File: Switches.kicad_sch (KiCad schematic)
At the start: 26 parts, among them J3 INDICATOR_SWITCH_OUT

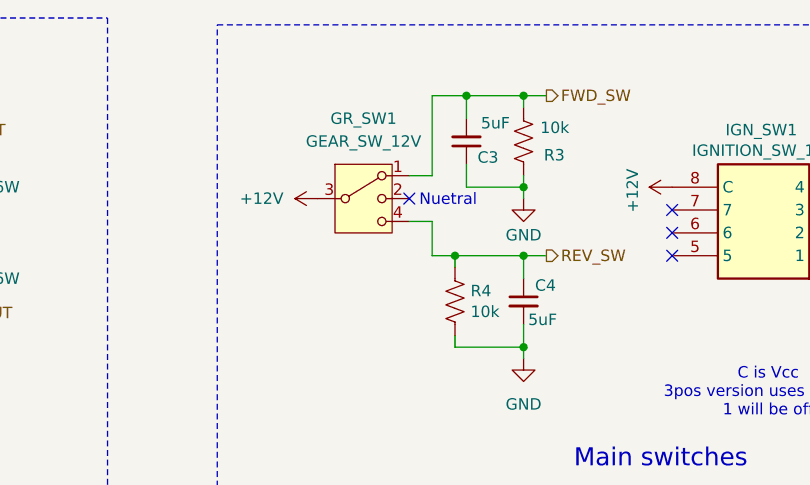
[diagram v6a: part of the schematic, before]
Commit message: Footprint all assigned, and updated to PCB
Ready for a check in to make sure everything is looking alright
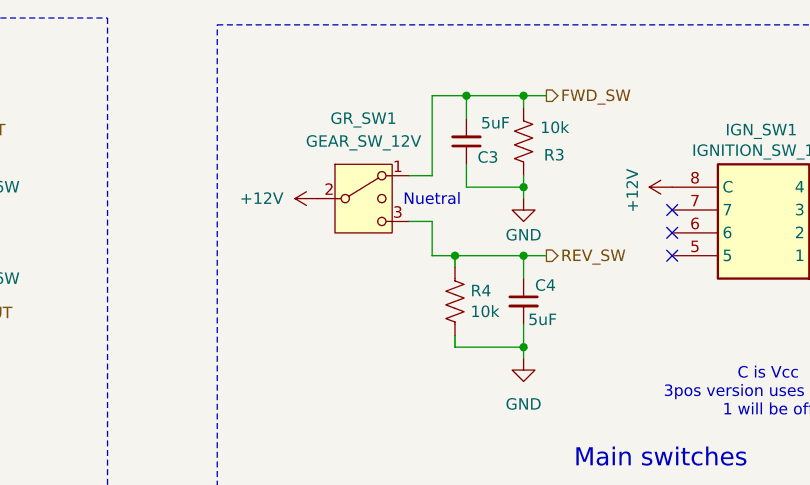
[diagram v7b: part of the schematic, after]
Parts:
- GR_SW1: symbol Switch:SW_SP3T -> Switch:SW_SPDT_MSM
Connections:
- net +12V: now also GR_SW1.2 (3); no longer GR_SW1.3
- net REV_SW: now also GR_SW1.3 (4); no longer GR_SW1.4
- no-connect marks 6 -> 5
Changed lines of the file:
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@@
 		(at 203.2 55.88)
-	)
-	(no_connect
-		(at 173.99 49.53)
 	)
 	(wire
@@
 	(text "Nuetral"
 		(exclude_from_sim no)
-		(at 178.308 49.784 0)
+		(at 176.53 49.784 0)
 		(effects
 			(font
@@
 	)
 	(symbol
-		(lib_id "Switch:SW_SP3T")
+		(lib_id "Switch:SW_SPDT_MSM")
 		(at 168.91 49.53 0)
 		(unit 1)
@@
 		)
 		(property "Footprint" "switched:SW_100_SP3T-Vertical"
-			(at 153.035 45.085 0)
+			(at 154.94 38.1 0)
 			(effects
 				(font
@@
 			)
 		)
-		(property "Description" "Switch, three position, single pole triple throw, 3 position switch, SP3T"
+		(property "Description" "Switch, single pole double throw, center OFF position"
 			(at 168.91 49.53 0)
 			(effects
@@
 		(pin "1"
 		)
-		(pin "4"
-		)
 		(instances

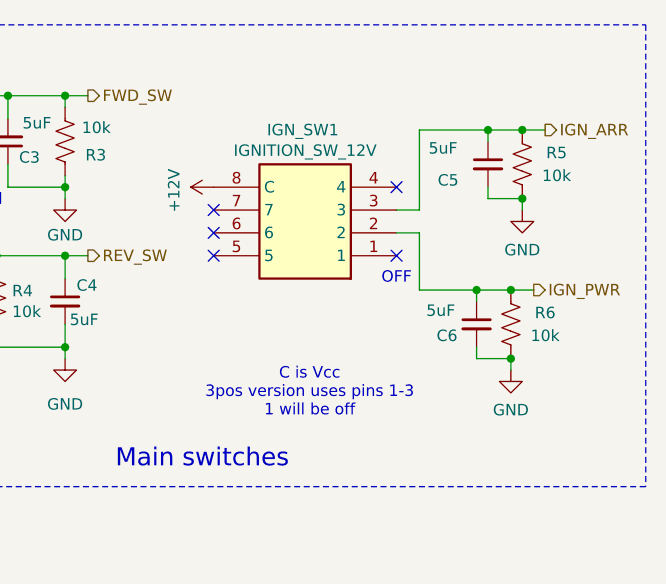
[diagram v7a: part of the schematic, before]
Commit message: Fixed fan and rot switch
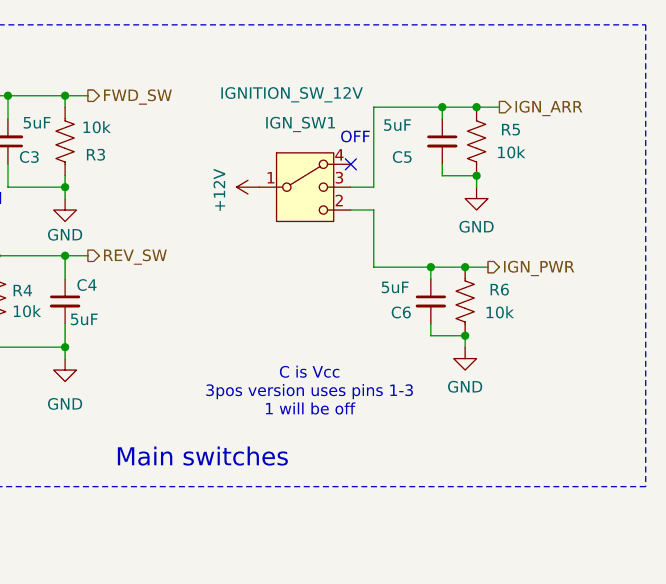
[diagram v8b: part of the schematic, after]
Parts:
- IGN_SW1: footprint switched:SW_ROT_3POS -> switched:SW_3POS_ROT; symbol RM103772BCB:RM103772BCB -> Switch:SW_SP3T
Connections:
- net +12V: now also IGN_SW1.1; no longer IGN_SW1.8 (C)
- no-connect marks 5 -> 1
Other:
- moved on the sheet: C5, C6, R5, R6
